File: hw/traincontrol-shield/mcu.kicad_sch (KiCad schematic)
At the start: 7 parts, among them J1 ESP32-S3 Header L, J2 ESP32-S3 Header R

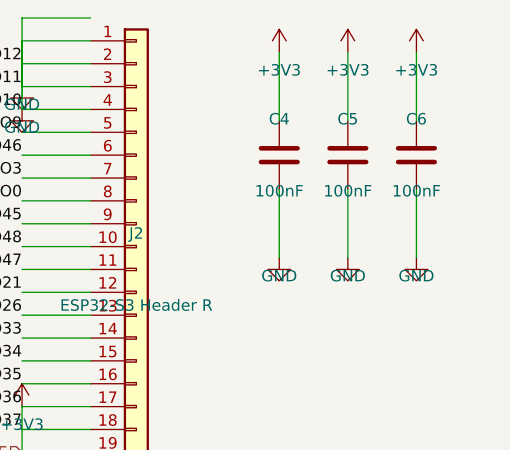
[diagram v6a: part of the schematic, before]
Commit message: Increase component spacing to eliminate pin-wire overlaps
- zero-crossing: move R1 left 7.62mm, add bridge wire to U2 pin2
- xor-interlock: move C10 right of U3 output (76→91mm), move C11 right (168→178mm)
- opto-triac: add 7.62mm COMP_GAP between MOC3021 and LED/gate resistors
- triacs-snubbers: move snubber column right (99→109mm), add 7.62mm gap between R and C
- mcu: widen C4/C5/C6 decap spacing from 7.62mm to 10.16mm
- power-supply: move R13 down 7.62mm, add bridge wire to R12

Co-Authored-By: Claude Sonnet 4.6 <noreply@anthropic.com>
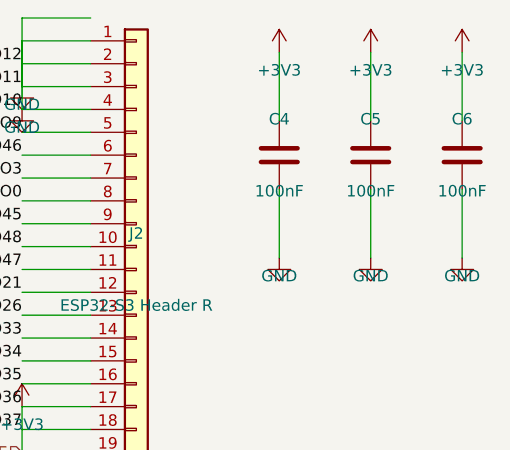
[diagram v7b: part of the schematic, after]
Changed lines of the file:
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@@
 	(symbol
 		(lib_id "Device:C")
-		(at 223.52 107.95 180)
+		(at 226.06 107.95 180)
 		(unit 1)
 		(exclude_from_sim no)
@@
 		(dnp no)
 		(property "Reference" "C5"
-			(at 223.52 103.95 0)
+			(at 226.06 103.95 0)
 			(effects (font (size 1.27 1.27)))
 		)
 		(property "Value" "100nF"
-			(at 223.52 111.95 0)
+			(at 226.06 111.95 0)
 			(effects (font (size 1.27 1.27)))
 		)
 		(property "Footprint" "Capacitor_SMD:C_0603_1608Metric"
-			(at 223.52 107.95 0)
+			(at 226.06 107.95 0)
 			(effects (font (size 1.27 1.27)) (hide yes))
 		)
 		(property "Datasheet" "~"
-			(at 223.52 107.95 0)
+			(at 226.06 107.95 0)
 			(effects (font (size 1.27 1.27)) (hide yes))
 		)
@@
 	)
 	(wire
-		(pts (xy 223.52 104.14) (xy 223.52 96.52))
+		(pts (xy 226.06 104.14) (xy 226.06 96.52))
 		(stroke (width 0) (type solid))
 	)
 	(symbol
 		(lib_id "power:+3V3")
-		(at 223.52 96.52 0)
+		(at 226.06 96.52 0)
 		(unit 1)
 		(exclude_from_sim no)
@@
 		(dnp no)
 		(property "Reference" "#PWR0811"
-			(at 223.52 94.52 0)
+			(at 226.06 94.52 0)
 			(effects (font (size 1.27 1.27)) (hide yes))
 		)
 		(property "Value" "+3V3"
-			(at 223.52 98.52 0)
-			(effects (font (size 1.27 1.27)))
-		)
-		(property "Footprint" ""
-			(at 223.52 96.52 0)
-			(effects (font (size 1.27 1.27)) (hide yes))
-		)
-		(property "Datasheet" ""
-			(at 223.52 96.52 0)
+			(at 226.06 98.52 0)
+			(effects (font (size 1.27 1.27)))
+		)
+		(property "Footprint" ""
+			(at 226.06 96.52 0)
+			(effects (font (size 1.27 1.27)) (hide yes))
+		)
+		(property "Datasheet" ""
+			(at 226.06 96.52 0)
 			(effects (font (size 1.27 1.27)) (hide yes))
 		)
@@
 	)
 	(wire
-		(pts (xy 223.52 111.76) (xy 223.52 119.38000000000001))
+		(pts (xy 226.06 111.76) (xy 226.06 119.38000000000001))
 		(stroke (width 0) (type solid))
 	)
 	(symbol
 		(lib_id "power:GND")
-		(at 223.52 119.38000000000001 0)
+		(at 226.06 119.38000000000001 0)
 		(unit 1)
 		(exclude_from_sim no)
@@
 		(dnp no)
 		(property "Reference" "#PWR0812"
-			(at 223.52 117.38000000000001 0)
+			(at 226.06 117.38000000000001 0)
 			(effects (font (size 1.27 1.27)) (hide yes))
 		)
 		(property "Value" "GND"
-			(at 223.52 121.38000000000001 0)
-			(effects (font (size 1.27 1.27)))
-		)
-		(property "Footprint" ""
-			(at 223.52 119.38000000000001 0)
-			(effects (font (size 1.27 1.27)) (hide yes))
-		)
-		(property "Datasheet" ""
-			(at 223.52 119.38000000000001 0)
+			(at 226.06 121.38000000000001 0)
+			(effects (font (size 1.27 1.27)))
+		)
+		(property "Footprint" ""
+			(at 226.06 119.38000000000001 0)
+			(effects (font (size 1.27 1.27)) (hide yes))
+		)
+		(property "Datasheet" ""
+			(at 226.06 119.38000000000001 0)
 			(effects (font (size 1.27 1.27)) (hide yes))
 		)
@@
 	(symbol
 		(lib_id "Device:C")
-		(at 231.14 107.95 180)
+		(at 236.22 107.95 180)
 		(unit 1)
 		(exclude_from_sim no)
@@
 		(dnp no)
 		(property "Reference" "C6"
-			(at 231.14 103.95 0)
+			(at 236.22 103.95 0)
 			(effects (font (size 1.27 1.27)))
 		)
 		(property "Value" "100nF"
-			(at 231.14 111.95 0)
+			(at 236.22 111.95 0)
 			(effects (font (size 1.27 1.27)))
 		)
 		(property "Footprint" "Capacitor_SMD:C_0603_1608Metric"
-			(at 231.14 107.95 0)
+			(at 236.22 107.95 0)
 			(effects (font (size 1.27 1.27)) (hide yes))
 		)
 		(property "Datasheet" "~"
-			(at 231.14 107.95 0)
+			(at 236.22 107.95 0)
 			(effects (font (size 1.27 1.27)) (hide yes))
 		)
@@
 	)
 	(wire
-		(pts (xy 231.14 104.14) (xy 231.14 96.52))
+		(pts (xy 236.22 104.14) (xy 236.22 96.52))
 		(stroke (width 0) (type solid))
 	)
 	(symbol
 		(lib_id "power:+3V3")
-		(at 231.14 96.52 0)
+		(at 236.22 96.52 0)
 		(unit 1)
 		(exclude_from_sim no)
@@
 		(dnp no)
 		(property "Reference" "#PWR0813"
-			(at 231.14 94.52 0)
+			(at 236.22 94.52 0)
 			(effects (font (size 1.27 1.27)) (hide yes))
 		)
 		(property "Value" "+3V3"
-			(at 231.14 98.52 0)
-			(effects (font (size 1.27 1.27)))
-		)
-		(property "Footprint" ""
-			(at 231.14 96.52 0)
-			(effects (font (size 1.27 1.27)) (hide yes))
-		)
-		(property "Datasheet" ""
-			(at 231.14 96.52 0)
+			(at 236.22 98.52 0)
+			(effects (font (size 1.27 1.27)))
+		)
+		(property "Footprint" ""
+			(at 236.22 96.52 0)
+			(effects (font (size 1.27 1.27)) (hide yes))
+		)
+		(property "Datasheet" ""
+			(at 236.22 96.52 0)
 			(effects (font (size 1.27 1.27)) (hide yes))
 		)
@@
 	)
 	(wire
-		(pts (xy 231.14 111.76) (xy 231.14 119.38000000000001))
+		(pts (xy 236.22 111.76) (xy 236.22 119.38000000000001))
 		(stroke (width 0) (type solid))
 	)
 	(symbol
 		(lib_id "power:GND")
-		(at 231.14 119.38000000000001 0)
+		(at 236.22 119.38000000000001 0)
 		(unit 1)
 		(exclude_from_sim no)
@@
 		(dnp no)
 		(property "Reference" "#PWR0814"
-			(at 231.14 117.38000000000001 0)
+			(at 236.22 117.38000000000001 0)
 			(effects (font (size 1.27 1.27)) (hide yes))
 		)
 		(property "Value" "GND"
-			(at 231.14 121.38000000000001 0)
-			(effects (font (size 1.27 1.27)))
-		)
-		(property "Footprint" ""
-			(at 231.14 119.38000000000001 0)
-			(effects (font (size 1.27 1.27)) (hide yes))
-		)
-		(property "Datasheet" ""
-			(at 231.14 119.38000000000001 0)
-			(effects (font (size 1.27 1.27)) (hide yes))
-		)
+			(at 236.22 121.38000000000001 0)
+			(effects (font (size 1.27 1.27)))
+		)
+		(property "Footprint" ""
+			(at 236.22 119.38000000000001 0)
+			(effects (font (size 1.27 1.27)) (hide yes))
+		)
+		(property "Datasheet" ""
+			(at 236.22 119.38000000000001 0)
+			(effects (font (size 1.27 1.27)) (hide yes))
+		)
